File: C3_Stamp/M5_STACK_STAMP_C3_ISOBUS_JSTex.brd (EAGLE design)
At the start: 53.3 x 30.5 mm, 13 parts, among them IC1 MCP2562-E_P, J1 61300811121, J2 61300611121, X1 S4P-VH

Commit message: 3 Versions.
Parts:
- removed J1: 61300811121, Wurth_Connectors_WR-PHD:61300811121
- added J3: 61301621821, Wurth_Connectors_WR-PHD:61301621821
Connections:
- net +3V3: now also J3.3
- net +5V: now also J3.15, J3.16; no longer J1.8
- net G10: now also J3.13, J3.14; no longer J1.7
- net G4: now also J3.4; no longer J1.2
- net G5: now also J3.5, J3.6; no longer J1.3
- net G6: now also J3.7, J3.8; no longer J1.4
- net G7: now also J3.10, J3.9; no longer J1.5
- net G8: now also J3.11, J3.12; no longer J1.6
- net GND: now also J3.1, J3.2; no longer J1.1
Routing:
- net +3V3: track 20.9 -> 42.3 mm
- net G8: track 0.00 -> 2.54 mm
- net G7: track 0.00 -> 2.54 mm
- net G6: track 0.00 -> 2.54 mm
- net G5: track 0.00 -> 2.54 mm
- net G10: track 0.00 -> 2.54 mm
- net +5V: track 60.9 -> 63.5 mm
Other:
- board size 53.3 x 30.5 mm -> 55.9 x 30.5 mm

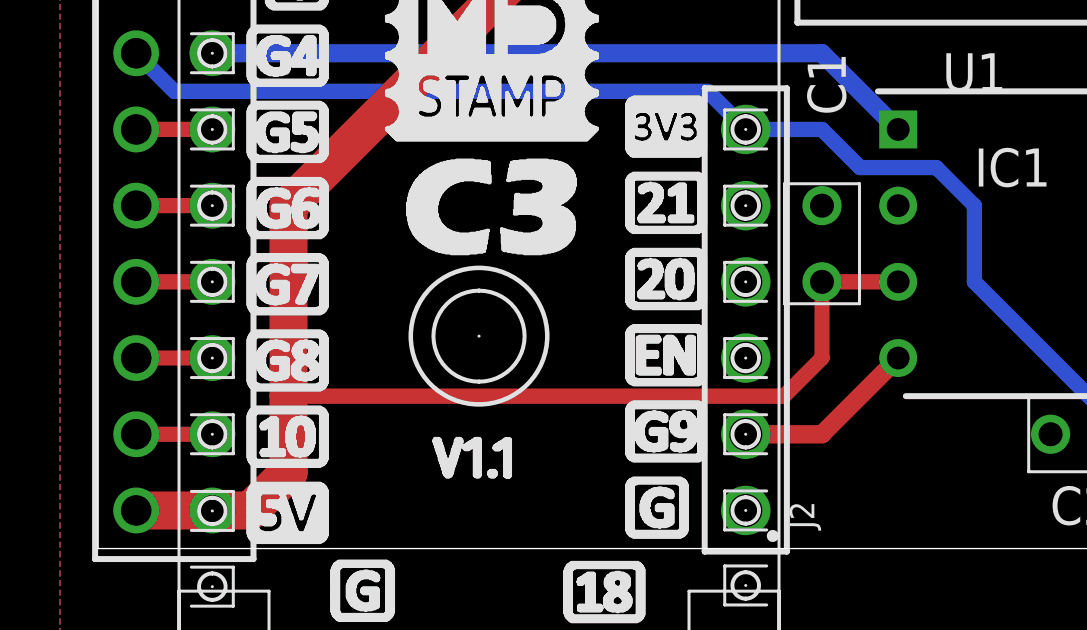
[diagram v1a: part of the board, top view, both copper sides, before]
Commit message: G7 for CAN RX, as G9 is a Strapping Pin.
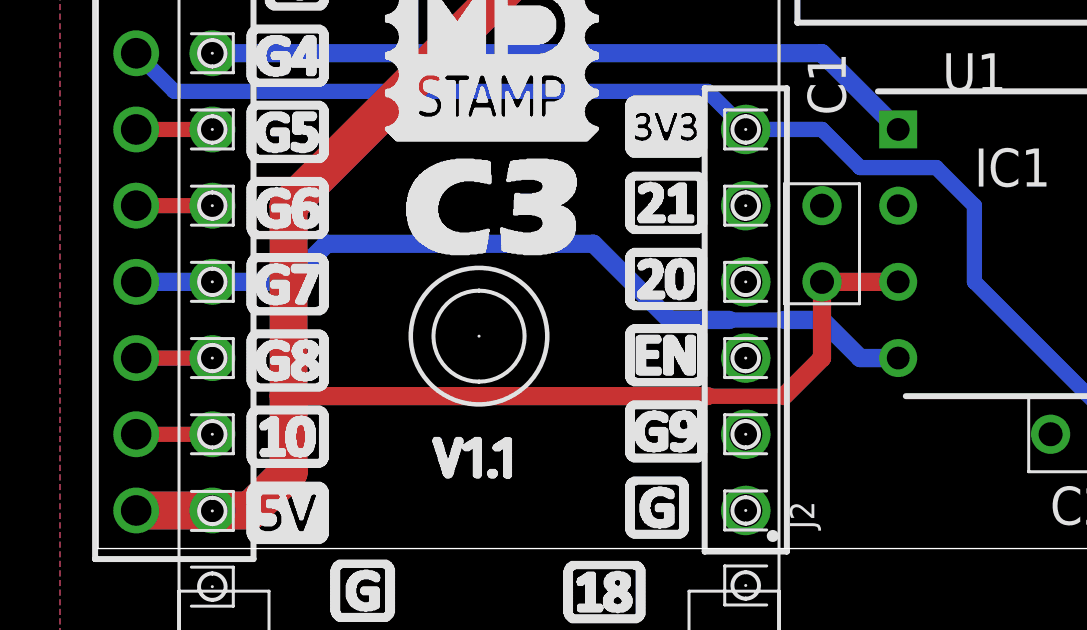
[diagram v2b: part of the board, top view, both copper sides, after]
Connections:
- net G7: now also IC1.4
- net G9: no longer IC1.4
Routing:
- net G7: track 2.54 -> 27.5 mm
- net G9: track 6.13 -> 0.00 mm
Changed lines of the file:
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@@
 <contactref element="IC1" pad="3"/>
 <wire x1="20.32" y1="25.4" x2="25.4" y2="25.4" width="1.27" layer="1"/>
-<wire x1="22.86" y1="10.16" x2="25.4" y2="10.16" width="0.508" layer="1"/>
-<wire x1="22.86" y1="10.16" x2="22.86" y2="7.62" width="0.508" layer="1"/>
-<wire x1="22.86" y1="7.62" x2="21.59" y2="6.35" width="0.508" layer="1"/>
-<wire x1="21.59" y1="6.35" x2="5.08" y2="6.35" width="0.508" layer="1"/>
+<wire x1="22.86" y1="10.16" x2="25.4" y2="10.16" width="0.6096" layer="1"/>
+<wire x1="22.86" y1="10.16" x2="22.86" y2="7.62" width="0.6096" layer="1"/>
+<wire x1="21.59" y1="6.35" x2="22.86" y2="7.62" width="0.6096" layer="1"/>
 <wire x1="2.54" y1="2.54" x2="3.81" y2="2.54" width="1.27" layer="1"/>
 <wire x1="3.81" y1="2.54" x2="5.08" y2="3.81" width="1.27" layer="1"/>
 <wire x1="5.08" y1="3.81" x2="5.08" y2="6.35" width="1.27" layer="1"/>
-<wire x1="5.08" y1="6.35" x2="5.08" y2="12.7" width="1.27" layer="1"/>
+<wire x1="5.08" y1="12.7" x2="5.08" y2="6.35" width="1.27" layer="1"/>
 <wire x1="5.08" y1="12.7" x2="17.78" y2="25.4" width="1.27" layer="1"/>
 <wire x1="17.78" y1="25.4" x2="20.32" y2="25.4" width="1.27" layer="1"/>
@@
 <contactref element="J3" pad="15"/>
 <wire x1="2.54" y1="2.54" x2="0" y2="2.54" width="1.27" layer="1"/>
+<wire x1="5.08" y1="6.35" x2="19.05" y2="6.35" width="0.6096" layer="1"/>
+<wire x1="19.05" y1="6.35" x2="21.59" y2="6.35" width="0.508" layer="1"/>
 </signal>
 <signal name="+3V3">
@@
 <signal name="G9">
 <contactref element="J2" pad="2"/>
-<contactref element="IC1" pad="4"/>
-<wire x1="20.32" y1="5.08" x2="22.86" y2="5.08" width="0.6096" layer="1"/>
-<wire x1="22.86" y1="5.08" x2="25.4" y2="7.62" width="0.6096" layer="1"/>
 </signal>
 <signal name="EN">
@@
 <contactref element="J3" pad="10"/>
 <contactref element="J3" pad="9"/>
-<wire x1="2.54" y1="10.16" x2="0" y2="10.16" width="0.508" layer="1"/>
+<contactref element="IC1" pad="4"/>
+<wire x1="0" y1="10.16" x2="2.54" y2="10.16" width="0.6096" layer="16"/>
+<wire x1="2.54" y1="10.16" x2="5.08" y2="10.16" width="0.6096" layer="16"/>
+<wire x1="5.08" y1="10.16" x2="6.35" y2="11.43" width="0.6096" layer="16"/>
+<wire x1="6.35" y1="11.43" x2="15.24" y2="11.43" width="0.6096" layer="16"/>
+<wire x1="15.24" y1="11.43" x2="17.78" y2="8.89" width="0.6096" layer="16"/>
+<wire x1="17.78" y1="8.89" x2="19.77669375" y2="8.89" width="0.6096" layer="16"/>
+<wire x1="25.4" y1="7.62" x2="24.13" y2="7.62" width="0.6096" layer="16"/>
+<wire x1="24.13" y1="7.62" x2="22.86" y2="8.89" width="0.6096" layer="16"/>
+<wire x1="21.59" y1="8.89" x2="22.86" y2="8.89" width="0.6096" layer="16"/>
+<wire x1="19.77669375" y1="8.89" x2="21.59" y2="8.89" width="0.508" layer="16"/>
 </signal>
 <signal name="G6">
